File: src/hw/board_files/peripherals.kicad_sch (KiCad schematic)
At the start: 25 parts, among them J3 MSD-1-A, Q1 PMOS, U5 NEO-M9N, U6 BQ27427, U7 SHT30-DIS

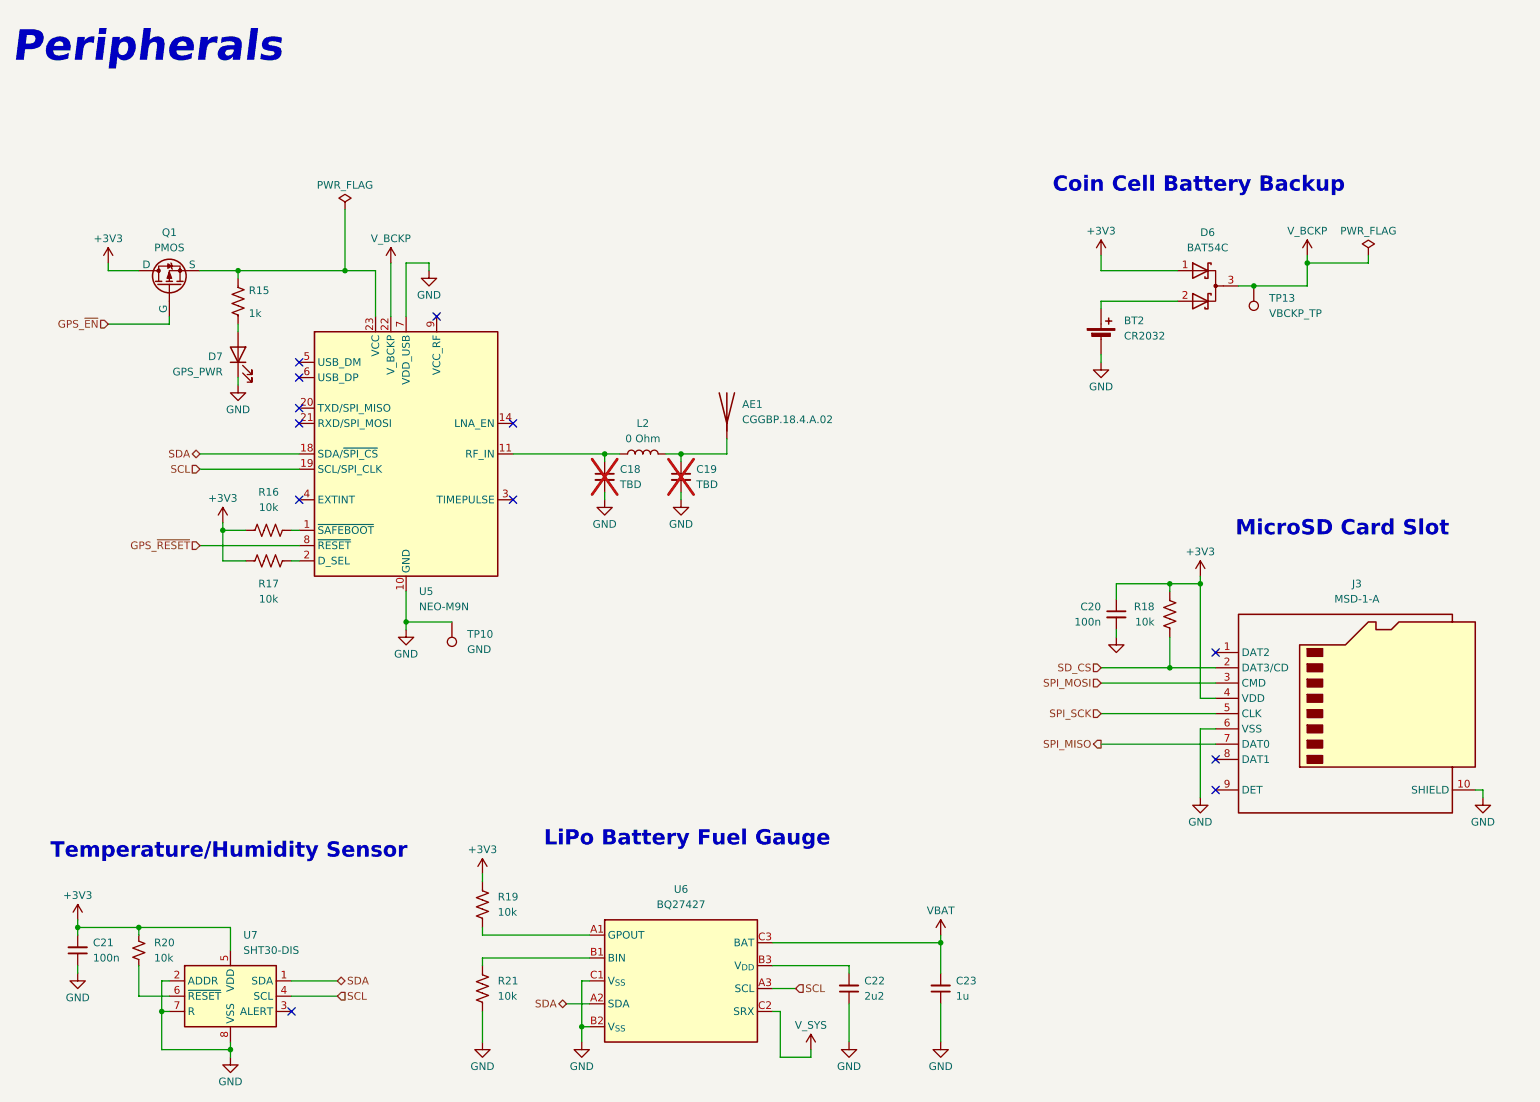
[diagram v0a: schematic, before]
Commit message: Added LCD to Schematic
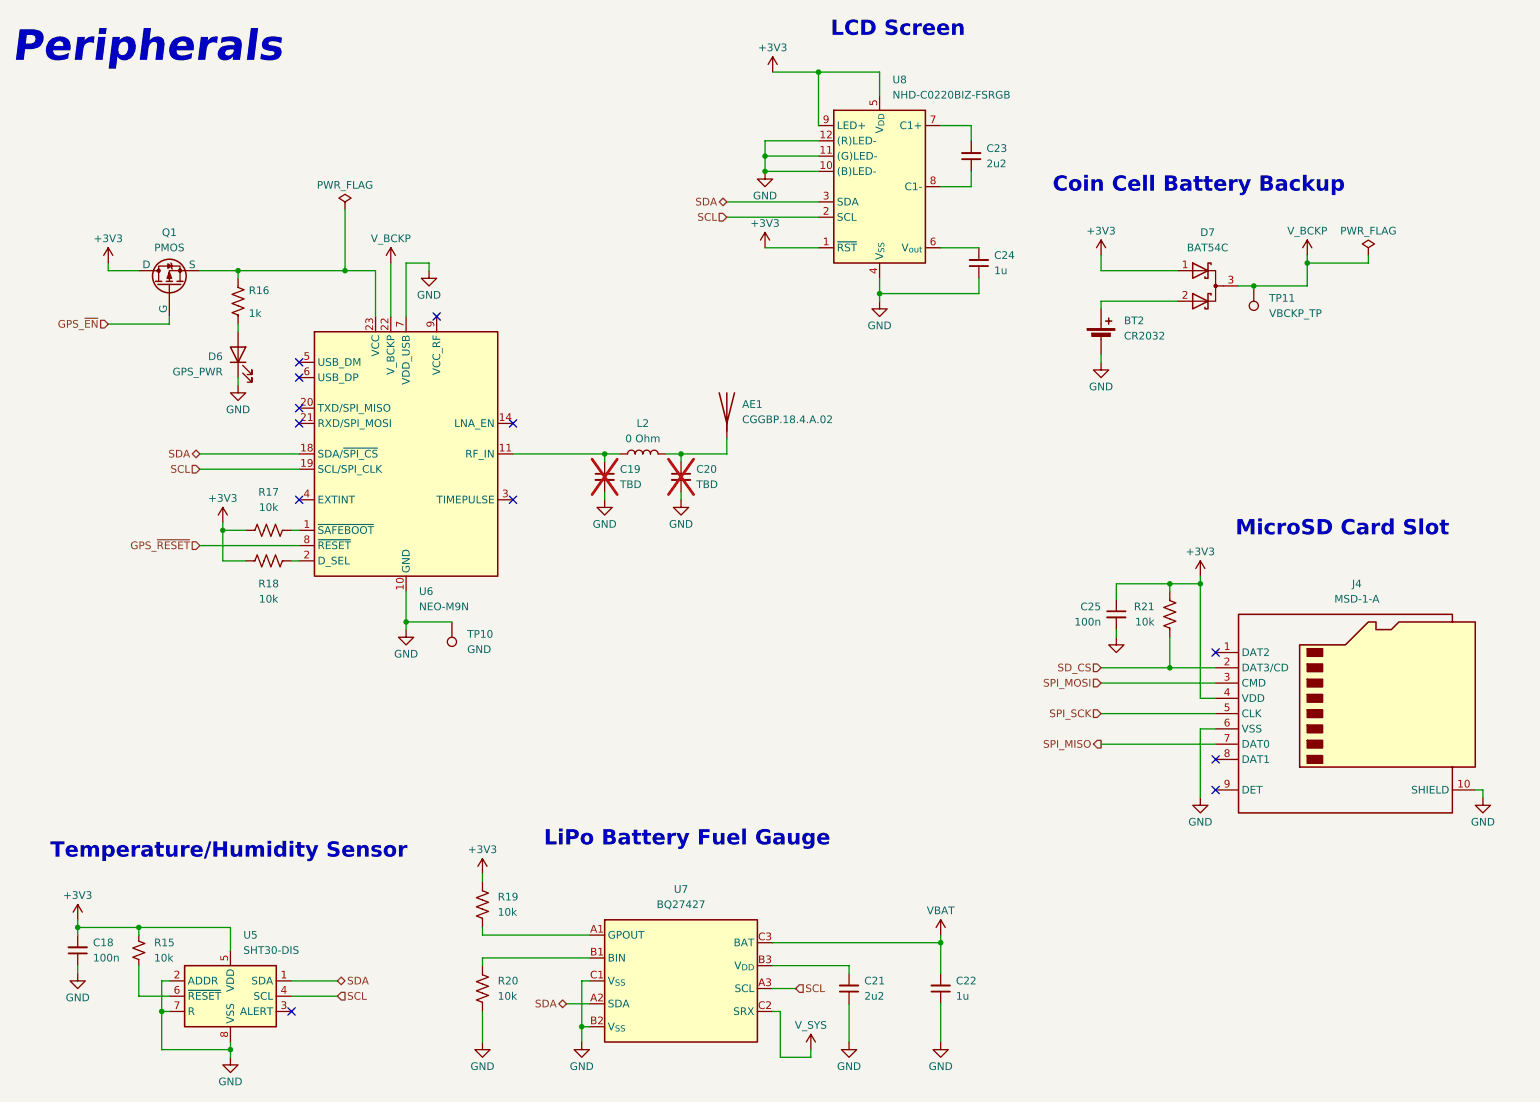
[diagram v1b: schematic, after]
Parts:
- added C23: 2u2, Capacitor_SMD:C_0603_1608Metric_Pad1.08x0.95mm_HandSolder, symbol Device:C_Small
- added C24: 1u, Capacitor_SMD:C_0603_1608Metric_Pad1.08x0.95mm_HandSolder, symbol Device:C_Small
- added U8: NHD-C0220BIZ-FSRGB, Display:NHD-C0220BiZ-FSRGB, symbol Display_Character:NHD-C0220BIZ-FSRGB
- renumbered C21 to C18, C18 to C19, C19 to C20, C22 to C21, C23 to C22, C20 to C25, D7 to D6, D6 to D7, J3 to J4, R20 to R15, R15 to R16, R16 to R17, R17 to R18, R21 to R20, R18 to R21, TP13 to TP11, U7 to U5, U5 to U6, U6 to U7
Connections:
- net +3V3: now also U8.1 (~{RST}), U8.5 (V_{DD}), U8.9 (LED+)
- net GND: now also C24.1, U8.10 ((B)LED-), U8.11 ((G)LED-), U8.12 ((R)LED-), U8.4 (V_{SS})
- net SCL: now also U8.2 (SCL)
- net SDA: now also U8.3 (SDA)
- new net: C24.2, U8.6 (V_{out})
- new net: C23.2, U8.7 (C1+)
- new net: C23.1, U8.8 (C1-)
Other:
- note added: "LCD Screen"

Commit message: Started BOM, changed micrsoSD card slot and some other footprint. Will need to update layout.
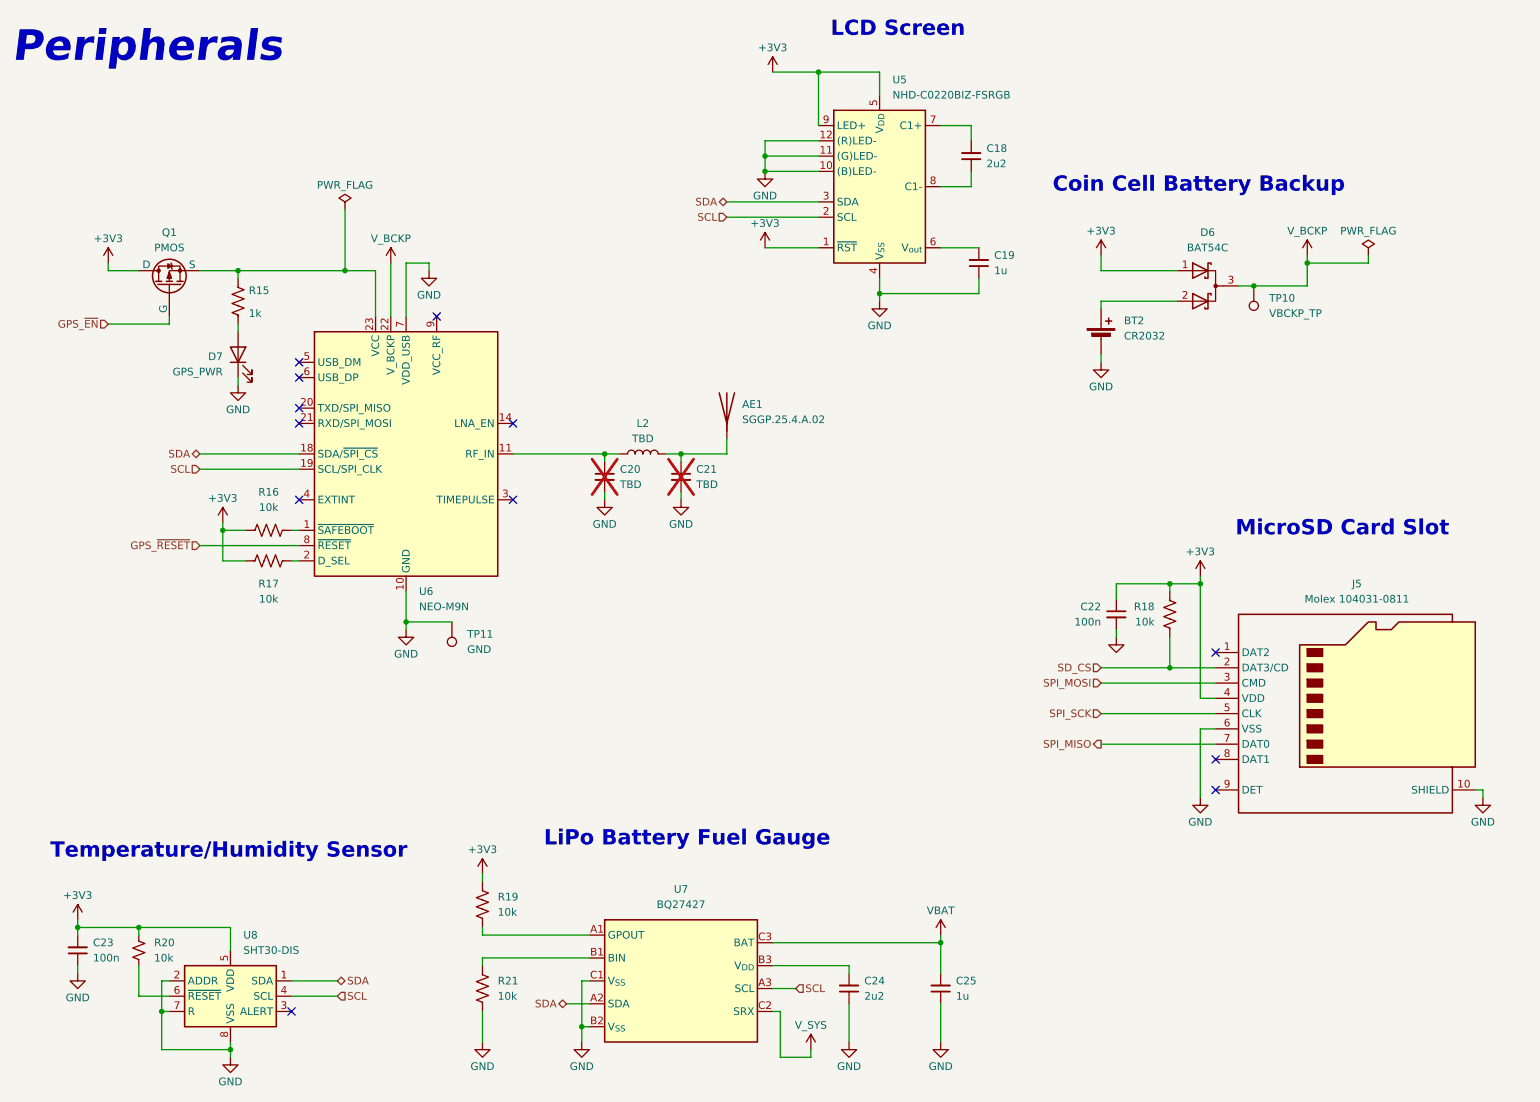
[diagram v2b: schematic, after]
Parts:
- AE1: value CGGBP.18.4.A.02 -> SGGP.25.4.A.02
- J5: renamed from J4; value MSD-1-A -> Molex 104031-0811; footprint Library:CUI_MSD-1-A -> Connector_Card:microSD_HC_Molex_104031-0811
- L2: value 0 Ohm -> TBD
- renumbered C23 to C18, C24 to C19, C19 to C20, C20 to C21, C25 to C22, C18 to C23, C21 to C24, C22 to C25, D7 to D6, D6 to D7, R16 to R15, R17 to R16, R18 to R17, R21 to R18, R15 to R20, R20 to R21, TP11 to TP10, TP10 to TP11, U8 to U5, U5 to U8

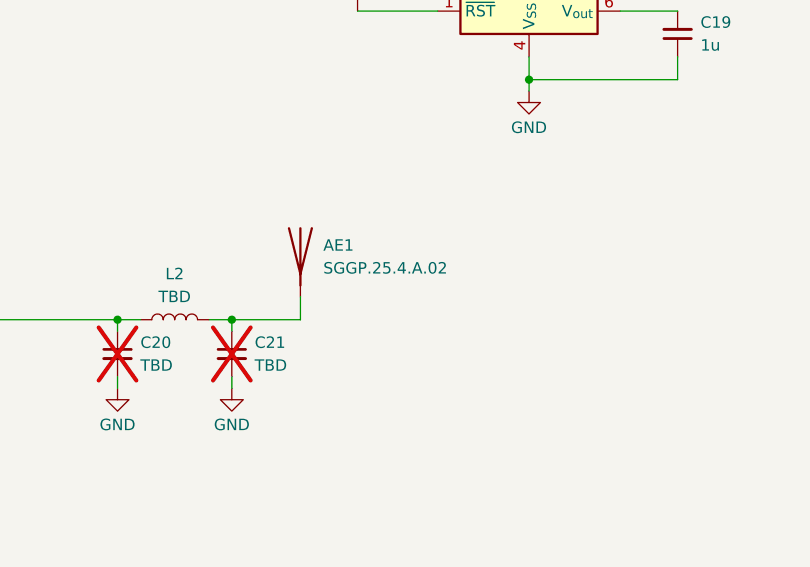
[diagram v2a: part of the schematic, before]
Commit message: Made antenna footprint. Making new branch to try new LCD and layout
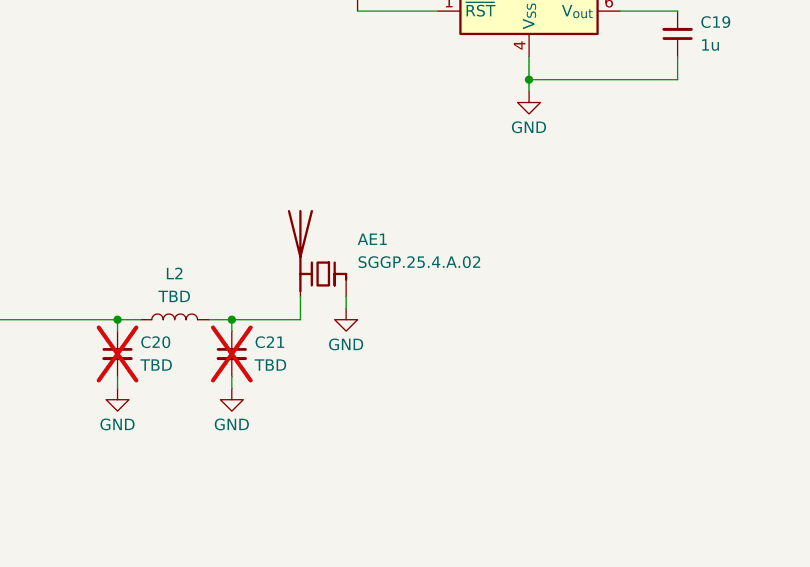
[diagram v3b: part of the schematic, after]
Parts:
- removed AE1: SGGP.25.4.A.02, symbol Device:Antenna
- added AE1: SGGP.25.4.A.02, Project_Library:Antenna_Taoglas_SGGP.25.4.A.02_25x25mm, symbol Device:Antenna_Chip
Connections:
- net GND: now also AE1.1 (FEED)
- net at C21.1, L2.2: now also AE1.2 (PCB_Trace)
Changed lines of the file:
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@@
 	(wire
 		(pts
+			(xy 138.43 83.82) (xy 138.43 85.09)
+		)
+		(stroke
+			(width 0)
+			(type default)
+		)
+	)
+	(wire
+		(pts
 			(xy 52.07 55.88) (xy 52.07 57.15)
 		)
@@
 	)
 	(symbol
+		(lib_id "Device:Antenna_Chip")
+		(at 135.89 81.28 0)
+		(mirror y)
+		(unit 1)
+		(exclude_from_sim no)
+		(in_bom yes)
+		(on_board yes)
+		(dnp no)
+		(fields_autoplaced yes)
+		(property "Reference" "AE1"
+			(at 139.7 77.4699 0)
+			(effects
+				(font
+					(size 1.27 1.27)
+				)
+				(justify right)
+			)
+		)
+		(property "Value" "SGGP.25.4.A.02"
+			(at 139.7 80.0099 0)
+			(effects
+				(font
+					(size 1.27 1.27)
+				)
+				(justify right)
+			)
+		)
+		(property "Footprint" "Project_Library:Antenna_Taoglas_SGGP.25.4.A.02_25x25mm"
+			(at 138.43 76.835 0)
+			(effects
+				(font
+					(size 1.27 1.27)
+				)
+				(hide yes)
+			)
+		)
+		(property "Datasheet" "https://cdn.taoglas.com/datasheets/SGGP.25.4.A.02.pdf"
+			(at 138.43 76.835 0)
+			(effects
+				(font
+					(size 1.27 1.27)
+				)
+				(hide yes)
+			)
+		)
+		(property "Description" "Ceramic chip antenna with pin for PCB trace"
+			(at 135.89 81.28 0)
+			(effects
+				(font
+					(size 1.27 1.27)
+				)
+				(hide yes)
+			)
+		)
+		(pin "1"
+		)
+		(pin "2"
+		)
+		(instances
+			(project ""
+				(path "/2c77a8ba-b277-4959-adec-d3fc778c7960/81382524-b053-4c3c-9e13-c8b314c52639"
+					(reference "AE1")
+					(unit 1)
+				)
+			)
+		)
+	)
+	(symbol
 		(lib_id "power:GND")
 		(at 25.4 172.72 0)
@@
 	)
 	(symbol
+		(lib_id "power:GND")
+		(at 138.43 85.09 0)
+		(unit 1)
+		(exclude_from_sim no)
+		(in_bom yes)
+		(on_board yes)
+		(dnp no)
+		(property "Reference" "#PWR080"
+			(at 138.43 91.44 0)
+			(effects
+				(font
+					(size 1.27 1.27)
+				)
+				(hide yes)
+			)
+		)
+		(property "Value" "GND"
+			(at 138.43 89.154 0)
+			(effects
+				(font
+					(size 1.27 1.27)
+				)
+			)
+		)
+		(property "Footprint" ""
+			(at 138.43 85.09 0)
+			(effects
+				(font
+					(size 1.27 1.27)
+				)
+				(hide yes)
+			)
+		)
+		(property "Datasheet" ""
+			(at 138.43 85.09 0)
+			(effects
+				(font
+					(size 1.27 1.27)
+				)
+				(hide yes)
+			)
+		)
+		(property "Description" "Power symbol creates a global label with name \"GND\" , ground"
+			(at 138.43 85.09 0)
+			(effects
+				(font
+					(size 1.27 1.27)
+				)
+				(hide yes)
+			)
+		)
+		(pin "1"
+		)
+		(instances
+			(project "pocket-caddy"
+				(path "/2c77a8ba-b277-4959-adec-d3fc778c7960/81382524-b053-4c3c-9e13-c8b314c52639"
+					(reference "#PWR080")
+					(unit 1)
+				)
+			)
+		)
+	)
+	(symbol
 		(lib_id "Device:D_Schottky_Dual_CommonCathode_AAK_Parallel")
 		(at 213.36 58.42 0)
@@
 					(unit 1)
 				)
-			)
-		)
-	)
-	(symbol
-		(lib_id "Device:Antenna")
-		(at 133.35 78.74 0)
-		(unit 1)
-		(exclude_from_sim no)
-		(in_bom yes)
-		(on_board yes)
-		(dnp no)
-		(fields_autoplaced yes)
-		(property "Reference" "AE1"
-			(at 135.89 78.1049 0)
-			(effects
-				(font
-					(size 1.27 1.27)
-				)
-				(justify left)
-			)
-		)
-		(property "Value" "SGGP.25.4.A.02"
-			(at 135.89 80.6449 0)
-			(effects
-				(font
-					(size 1.27 1.27)
-				)
-				(justify left)
-			)
-		)
-		(property "Footprint" ""
-			(at 133.35 78.74 0)
-			(effects
-				(font
-					(size 1.27 1.27)
-				)
-				(hide yes)
-			)
-		)
-		(property "Datasheet" "https://cdn.taoglas.com/datasheets/SGGP.25.4.A.02.pdf"
-			(at 133.35 78.74 0)
-			(effects
-				(font
-					(size 1.27 1.27)
-				)
-				(hide yes)
-			)
-		)
-		(property "Description" "Antenna"
-			(at 133.35 78.74 0)
-			(effects
-				(font
-					(size 1.27 1.27)
-				)
-				(hide yes)
-			)
-		)
-		(pin "1"
-		)
-		(instances
-			(project ""
-				(path "/2c77a8ba-b277-4959-adec-d3fc778c7960/81382524-b053-4c3c-9e13-c8b314c52639"
-					(reference "AE1")
-					(unit 1)
-				)

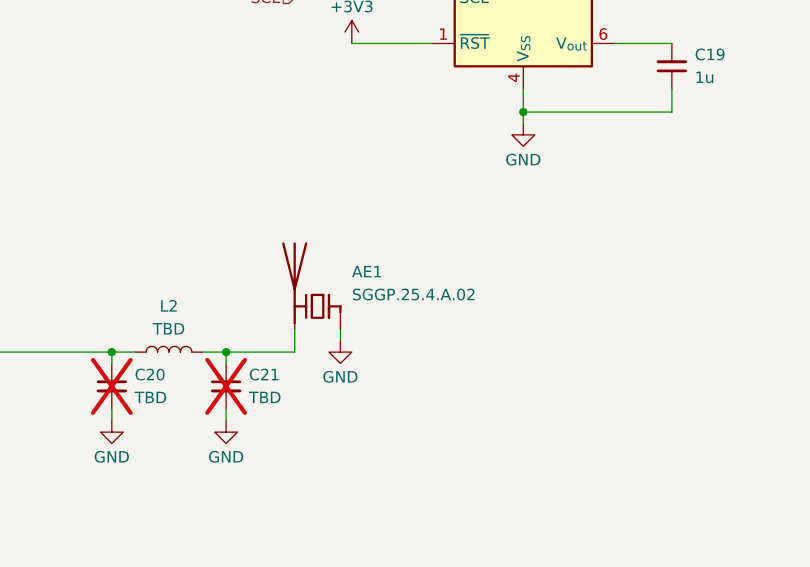
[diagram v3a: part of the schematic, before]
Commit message: Moved some things around, revised regulator layout
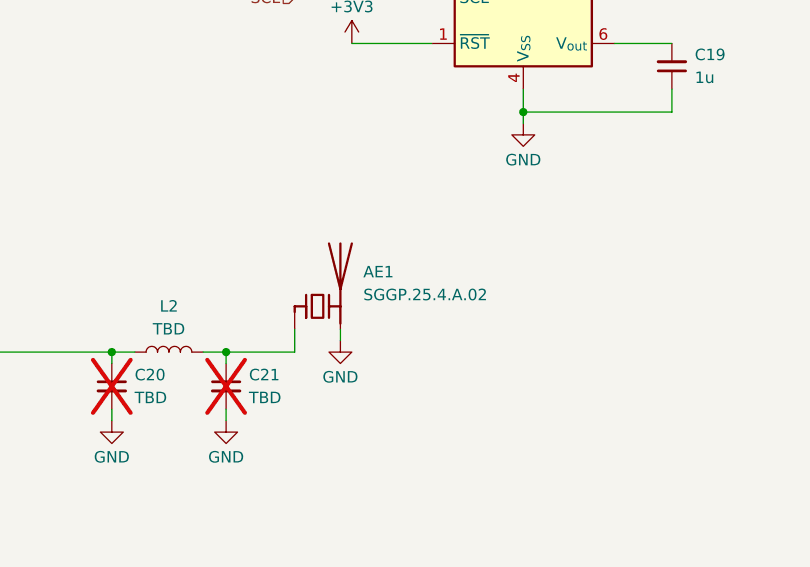
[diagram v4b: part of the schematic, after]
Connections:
- net GND: now also AE1.2 (PCB_Trace), AE1.MP; no longer AE1.1 (FEED)
- net at C21.1, L2.2: now also AE1.1 (FEED); no longer AE1.2 (PCB_Trace)
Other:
- moved on the sheet: AE1
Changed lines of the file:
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@@
 		(lib_id "Device:Antenna_Chip")
 		(at 135.89 81.28 0)
-		(mirror y)
 		(unit 1)
 		(exclude_from_sim no)
@@
 		(fields_autoplaced yes)
 		(property "Reference" "AE1"
-			(at 139.7 77.4699 0)
+			(at 140.97 77.4699 0)
 			(effects
 				(font
 					(size 1.27 1.27)
 				)
-				(justify right)
+				(justify left)
 			)
 		)
 		(property "Value" "SGGP.25.4.A.02"
-			(at 139.7 80.0099 0)
+			(at 140.97 80.0099 0)
 			(effects
 				(font
 					(size 1.27 1.27)
 				)
-				(justify right)
+				(justify left)
 			)
 		)
 		(property "Footprint" "Project_Library:Antenna_Taoglas_SGGP.25.4.A.02_25x25mm"
-			(at 138.43 76.835 0)
+			(at 133.35 76.835 0)
 			(effects
 				(font
@@
 		)
 		(property "Datasheet" "https://cdn.taoglas.com/datasheets/SGGP.25.4.A.02.pdf"
-			(at 138.43 76.835 0)
+			(at 133.35 76.835 0)
 			(effects
 				(font
@@
 		(pin "2"
 		)
+		(pin "MP"
+		)
 		(instances
